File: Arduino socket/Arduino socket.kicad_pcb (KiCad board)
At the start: 2 copper layers, 40.6 x 39.7 mm, 2 parts, among them J3 Conn_01x06_Socket

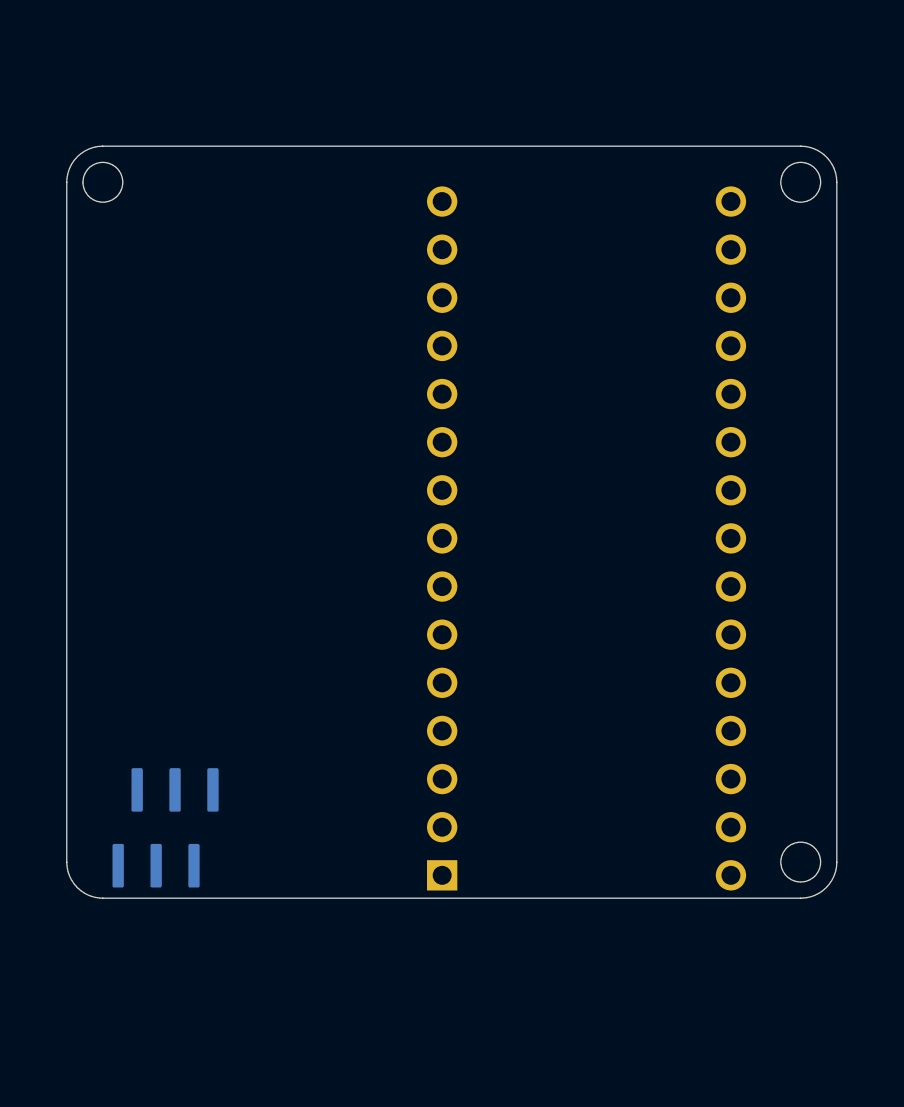
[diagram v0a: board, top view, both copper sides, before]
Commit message: Started coding.
Reading and writing to registers implemented.
The circuit is now on rev 1.1, but there were some mistakes on this one to, hehe.
The dip-switch is NOT the same size as a 16p soic, a little wider (bodgedd by bending pins under on one side (the one thats just all vcc anyways, as it can be bridged if you're struggeling with the jank solder)).
The socket also has some mechanical solder points on the ends, that wasnt on my footprint. They are also thinner and longer than thought. The mechanical solder on one side could short some pins on the 165, but i simply put a piece of kapton tape acrross the pins. Circuit works otherwise. Perhaps a little hot. Maybe not ideal to drive LEDs directly from 595's, but they can probably handle it
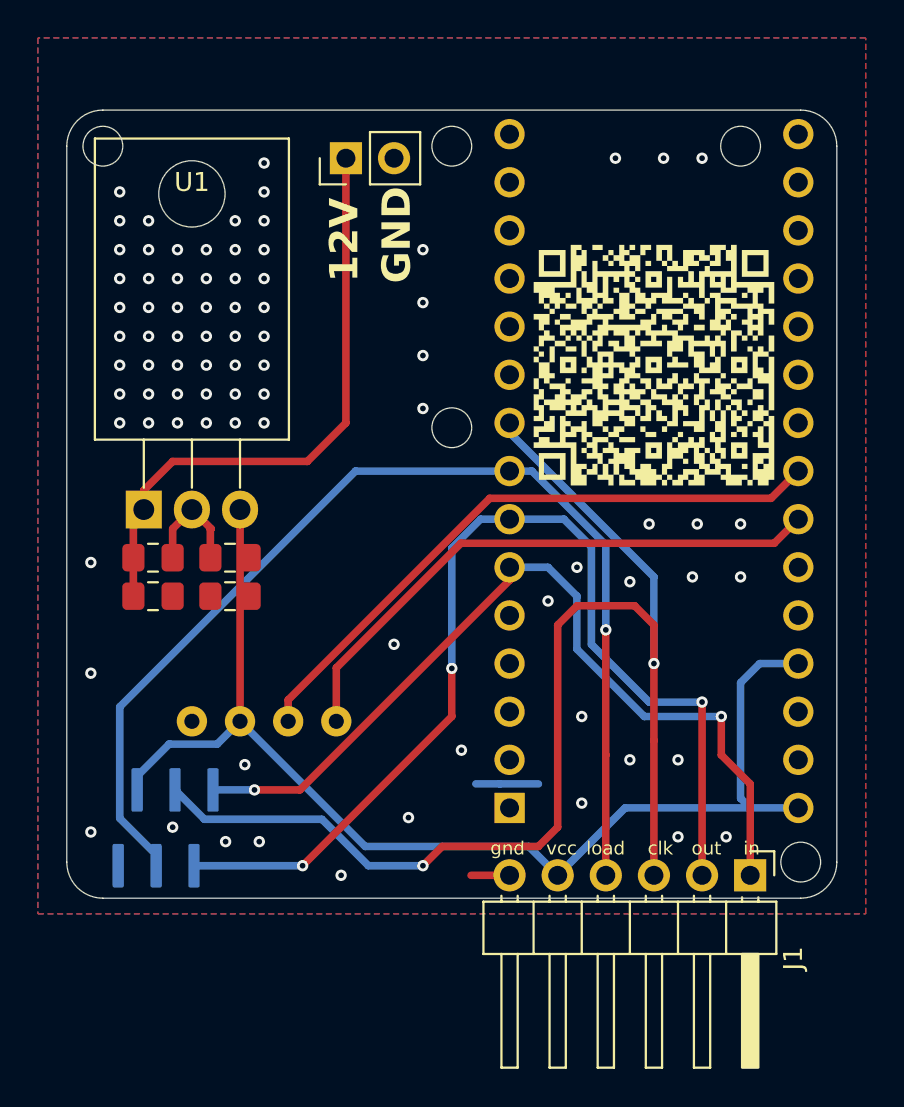
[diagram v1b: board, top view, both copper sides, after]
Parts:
- added C1: C, Capacitor_SMD:C_0805_2012Metric_Pad1.18x1.45mm_HandSolder, F.Cu at (111.2, 76.7)
- added C2: C, Capacitor_SMD:C_0805_2012Metric_Pad1.18x1.45mm_HandSolder, F.Cu at (111.2, 78.7)
- added C3: C, Capacitor_SMD:C_0805_2012Metric_Pad1.18x1.45mm_HandSolder, F.Cu at (115.3, 76.7)
- added C4: C, Capacitor_SMD:C_0805_2012Metric_Pad1.18x1.45mm_HandSolder, F.Cu at (115.3, 78.7)
- added G***: LOGO, LOGO, F.Cu at (137.7, 66.5)
- added J1: Conn_01x06_Pin, Connector_PinHeader_2.54mm:PinHeader_1x06_P2.54mm_Horizontal, F.Cu at (142.7, 93.5)
- added J2: Conn_01x02_Pin, Connector_PinHeader_2.54mm:PinHeader_1x02_P2.54mm_Vertical, F.Cu at (121.4, 55.6)
- added RTC1: ~, timezoneClock:DS3231 RTC module, F.Cu at (117.1, 67.6)
- added U1: L7805, Package_TO_SOT_THT:TO-220-3_Horizontal_TabDown, F.Cu at (110.7, 74.2)
- moved A1 5.03 mm to (130.0, 89.9)
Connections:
- A1 pad 23: unconnected-(A1-A4-Pad23) -> SDA
- A1 pad 24: unconnected-(A1-A5-Pad24) -> SCL
- A1 pad 29: unconnected-(A1-GND-Pad29) -> GND
- A1 pad 4: unconnected-(A1-GND-Pad4) -> GND
- A1 pad 6: unconnected-(A1-D3-Pad6) -> PISO in
- A1 pad 7: unconnected-(A1-D4-Pad7) -> SIPO out
- A1 pad 8: unconnected-(A1-D5-Pad8) -> Shift/load
- A1 pad 9: unconnected-(A1-D6-Pad9) -> Clock
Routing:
- net Clock: track 0.00 -> 68.3 mm, vias 0 -> 2
- net VCC: track 0.00 -> 63.1 mm
- net Shift/load: track 0.00 -> 59.0 mm, vias 0 -> 1
- net SIPO out: track 0.00 -> 55.8 mm, vias 0 -> 3
- net PISO in: track 0.00 -> 46.1 mm, vias 0 -> 2
- net SDA: track 0.00 -> 33.1 mm
- net Net-(J2-Pin_1): track 0.00 -> 31.9 mm
- net SCL: track 0.00 -> 30.5 mm
- net GND: track 0.00 -> 11.3 mm, vias 0 -> 81
- added copper zone on B.Cu, net GND
- added copper zone on F.Cu, net GND
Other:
- board size 40.6 x 39.7 mm -> 40.6 x 41.6 mm
- board text added: "12V"
- board text added: "GND"
- board text added: "clk"
- board text added: "gnd"
- board text added: "in"
- board text added: "load"
- board text added: "out"
- board text added: "vcc"
